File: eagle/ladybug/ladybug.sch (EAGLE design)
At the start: 4 parts

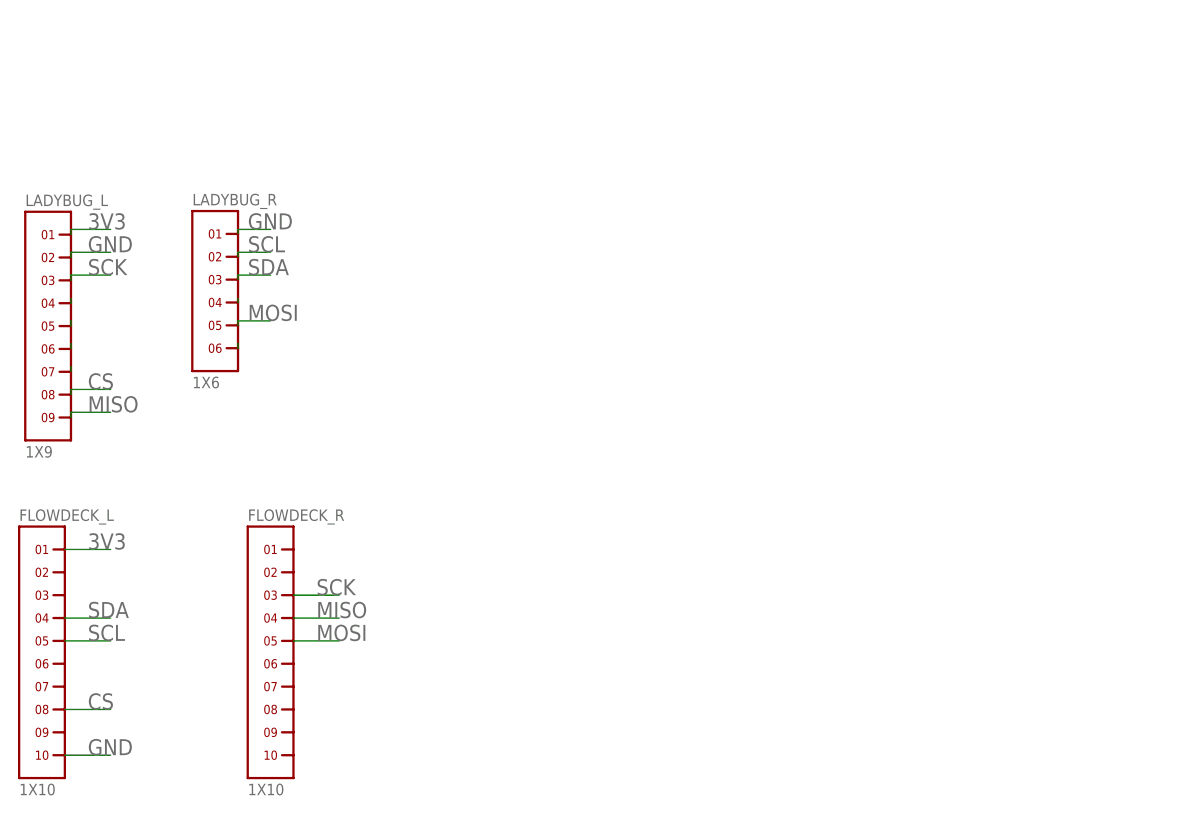
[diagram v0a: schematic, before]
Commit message: Added TinyPICO Nano to Ladybug board
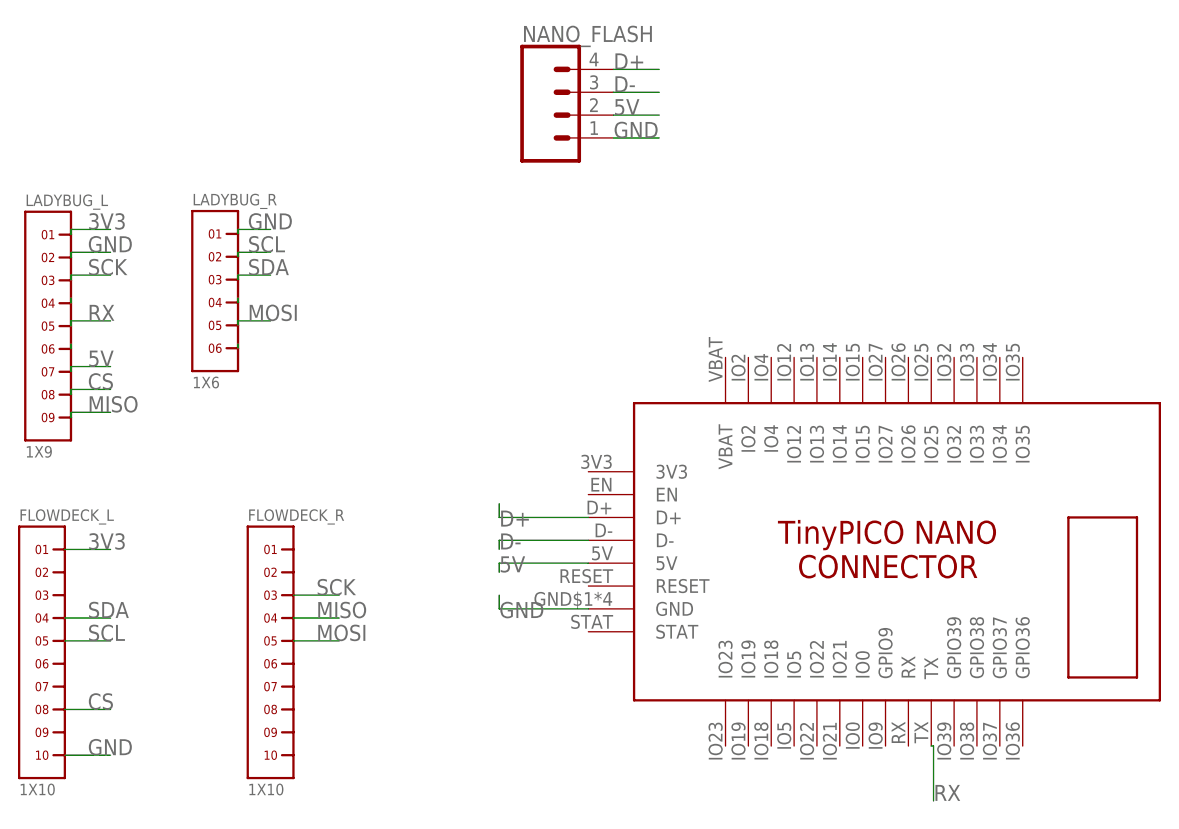
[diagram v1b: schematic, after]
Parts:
- added NANO_FLASH: (no value), SparkFun-Connectors:CONN_041X04_NO_SILK
- added U$1: TINYPICO-NANO-CONNECTOR, TinyPICO_NANO_Eagle:TINYPICO-NANO-CONNECTOR
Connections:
- removed net RX2: LADYBUG_L.5
- new net D+: NANO_FLASH.4, U$1.D+
- new net D-: NANO_FLASH.3, U$1.D-
- new net RX: LADYBUG_L.5, U$1.TX
- net 5V: now also NANO_FLASH.2, U$1.5V
- net GND: now also NANO_FLASH.1, U$1.GND
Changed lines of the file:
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@@
 <?xml version="1.0" encoding="utf-8"?>
 <!DOCTYPE eagle SYSTEM "eagle.dtd">
-<eagle version="9.1.1">
+<eagle version="9.6.2">
 <drawing>
 <settings>
@@
 <layer number="56" name="wert" color="7" fill="1" visible="no" active="no"/>
 <layer number="57" name="tCAD" color="7" fill="1" visible="no" active="no"/>
+<layer number="58" name="bCAD" color="7" fill="1" visible="no" active="no"/>
 <layer number="59" name="tCarbon" color="7" fill="1" visible="no" active="no"/>
 <layer number="60" name="bCarbon" color="7" fill="1" visible="no" active="no"/>
@@
 <layer number="115" name="ReferenceISLANDS" color="7" fill="1" visible="yes" active="yes"/>
 <layer number="116" name="Patch_BOT" color="9" fill="4" visible="yes" active="yes"/>
+<layer number="117" name="BACKMAAT1" color="7" fill="1" visible="no" active="no"/>
 <layer number="118" name="Rect_Pads" color="7" fill="1" visible="yes" active="yes"/>
+<layer number="119" name="KAP_TEKEN" color="7" fill="1" visible="no" active="no"/>
+<layer number="120" name="KAP_MAAT1" color="7" fill="1" visible="no" active="no"/>
 <layer number="121" name="_tsilk" color="7" fill="1" visible="yes" active="yes"/>
 <layer number="122" name="_bsilk" color="7" fill="1" visible="yes" active="yes"/>
@@
 <layer number="128" name="_bValues" color="7" fill="1" visible="yes" active="yes"/>
 <layer number="129" name="Mask" color="7" fill="1" visible="yes" active="yes"/>
+<layer number="130" name="SMDSTROOK" color="7" fill="1" visible="no" active="no"/>
 <layer number="131" name="tAdjust" color="7" fill="1" visible="yes" active="yes"/>
 <layer number="132" name="bAdjust" color="7" fill="1" visible="yes" active="yes"/>
+<layer number="133" name="bottom_silk" color="7" fill="1" visible="no" active="no"/>
+<layer number="134" name="silk_top" color="7" fill="1" visible="no" active="no"/>
+<layer number="135" name="silk_bottom" color="7" fill="1" visible="no" active="no"/>
+<layer number="136" name="silktop" color="7" fill="1" visible="yes" active="yes"/>
+<layer number="137" name="silkbottom" color="7" fill="1" visible="yes" active="yes"/>
+<layer number="138" name="mbTest" color="7" fill="1" visible="no" active="yes"/>
+<layer number="139" name="mtKeepout" color="7" fill="1" visible="no" active="yes"/>
+<layer number="140" name="mbKeepout" color="7" fill="1" visible="no" active="yes"/>
+<layer number="141" name="mtRestrict" color="7" fill="1" visible="no" active="yes"/>
+<layer number="142" name="mbRestrict" color="7" fill="1" visible="no" active="yes"/>
+<layer number="143" name="mvRestrict" color="7" fill="1" visible="no" active="yes"/>
 <layer number="144" name="Drill_legend" color="7" fill="1" visible="yes" active="yes"/>
+<layer number="145" name="DrillLegend_01-16" color="7" fill="1" visible="yes" active="yes"/>
+<layer number="146" name="DrillLegend_01-20" color="7" fill="1" visible="yes" active="yes"/>
+<layer number="147" name="mMeasures" color="7" fill="1" visible="no" active="yes"/>
+<layer number="148" name="mDocument" color="7" fill="1" visible="no" active="yes"/>
+<layer number="149" name="mReference" color="7" fill="1" visible="no" active="yes"/>
 <layer number="150" name="Notes" color="7" fill="1" visible="yes" active="yes"/>
 <layer number="151" name="HeatSink" color="7" fill="1" visible="yes" active="yes"/>
@@
 <layer number="154" name="FabDoc2" color="7" fill="1" visible="yes" active="yes"/>
 <layer number="155" name="FabDoc3" color="7" fill="1" visible="yes" active="yes"/>
+<layer number="156" name="gesam-Maß" color="7" fill="1" visible="no" active="no"/>
+<layer number="157" name="FaceMchng" color="7" fill="1" visible="no" active="no"/>
+<layer number="158" name="FaceMMeas" color="7" fill="1" visible="no" active="no"/>
+<layer number="159" name="Geh-Bear2" color="7" fill="1" visible="no" active="no"/>
+<layer number="160" name="Topologie" color="7" fill="1" visible="no" active="no"/>
+<layer number="161" name="tomplace2" color="7" fill="1" visible="no" active="no"/>
+<layer number="166" name="AntennaArea" color="7" fill="1" visible="yes" active="yes"/>
+<layer number="168" name="4mmHeightArea" color="7" fill="1" visible="yes" active="yes"/>
+<layer number="191" name="mNets" color="7" fill="1" visible="no" active="yes"/>
+<layer number="192" name="mBusses" color="7" fill="1" visible="no" active="yes"/>
+<layer number="193" name="mPins" color="7" fill="1" visible="no" active="yes"/>
+<layer number="194" name="mSymbols" color="7" fill="1" visible="no" active="yes"/>
+<layer number="195" name="mNames" color="7" fill="1" visible="no" active="yes"/>
+<layer number="196" name="mValues" color="7" fill="1" visible="no" active="yes"/>
 <layer number="199" name="Contour" color="7" fill="1" visible="yes" active="yes"/>
 <layer number="200" name="200bmp" color="1" fill="10" visible="yes" active="yes"/>
@@
 <layer number="250" name="Descript" color="3" fill="1" visible="no" active="no"/>
 <layer number="251" name="SMDround" color="12" fill="11" visible="no" active="no"/>
+<layer number="252" name="BR-BS" color="7" fill="1" visible="no" active="no"/>
+<layer number="253" name="Extra" color="7" fill="1" visible="no" active="no"/>
 <layer number="254" name="cooling" color="7" fill="1" visible="yes" active="yes"/>
 <layer number="255" name="routoute" color="7" fill="1" visible="yes" active="yes"/>
@@
 <part name="FLOWDECK_L" library="headers(2mm)" deviceset="1X10" device=""/>
 <part name="FLOWDECK_R" library="headers(2mm)" deviceset="1X10" device=""/>
+<part name="U$1" library="TinyPICO_NANO_Eagle" deviceset="TINYPICO-NANO-CONNECTOR" device=""/>
+<part name="NANO_FLASH" library="SparkFun-Connectors" deviceset="CONN_04" device="1X04_NO_SILK"/>
 </parts>
 <sheets>
@@
 <attribute name="VALUE" x="10.16" y="18.415" size="1.27" layer="96" font="vector"/>
 </instance>
+<instance part="U$1" gate="G$1" x="81.28" y="45.72" smashed="yes"/>
+<instance part="NANO_FLASH" gate="J1" x="45.72" y="93.98" smashed="yes">
+<attribute name="VALUE" x="40.64" y="86.614" size="1.778" layer="96" font="vector"/>
+<attribute name="NAME" x="40.64" y="102.108" size="1.778" layer="95" font="vector"/>
+</instance>
 </instances>
 <busses>
@@
 <pinref part="LADYBUG_L" gate="G$1" pin="7"/>
 <wire x1="-9.48" y1="65.46" x2="-9.48" y2="66.04" width="0.1524" layer="91"/>
-</segment>
-</net>
-<net name="RX2" class="0">
+<wire x1="-9.48" y1="66.04" x2="-5.08" y2="66.04" width="0.1524" layer="91"/>
+<label x="-7.62" y="66.04" size="1.778" layer="95"/>
+</segment>
+<segment>
+<pinref part="U$1" gate="G$1" pin="5V"/>
+<wire x1="48.006" y1="44.196" x2="38.1" y2="44.196" width="0.1524" layer="91"/>
+<wire x1="38.1" y1="44.196" x2="38.1" y2="43.18" width="0.1524" layer="91"/>
+<label x="38.1" y="43.18" size="1.778" layer="95"/>
+</segment>
+<segment>
+<pinref part="NANO_FLASH" gate="J1" pin="2"/>
+<wire x1="50.8" y1="93.98" x2="55.88" y2="93.98" width="0.1524" layer="91"/>
+<label x="50.8" y="93.98" size="1.778" layer="95"/>
+</segment>
+</net>
+<net name="RX" class="0">
 <segment>
 <pinref part="LADYBUG_L" gate="G$1" pin="5"/>
 <wire x1="-9.48" y1="70.54" x2="-9.48" y2="71.12" width="0.1524" layer="91"/>
+<wire x1="-9.48" y1="71.12" x2="-5.08" y2="71.12" width="0.1524" layer="91"/>
+<label x="-7.62" y="71.12" size="1.778" layer="95"/>
+</segment>
+<segment>
+<pinref part="U$1" gate="G$1" pin="TX"/>
+<wire x1="86.106" y1="23.876" x2="86.36" y2="23.876" width="0.1524" layer="91"/>
+<wire x1="86.36" y1="23.876" x2="86.36" y2="17.78" width="0.1524" layer="91"/>
+<label x="86.36" y="17.78" size="1.778" layer="95"/>
 </segment>
 </net>
@@
 <label x="-7.62" y="22.86" size="1.778" layer="95"/>
 </segment>
+<segment>
+<pinref part="U$1" gate="G$1" pin="GND"/>
+<wire x1="48.006" y1="39.116" x2="38.1" y2="39.116" width="0.1524" layer="91"/>
+<wire x1="38.1" y1="39.116" x2="38.1" y2="40.64" width="0.1524" layer="91"/>
+<label x="38.1" y="38.1" size="1.778" layer="95"/>
+</segment>
+<segment>
+<pinref part="NANO_FLASH" gate="J1" pin="1"/>
+<wire x1="50.8" y1="91.44" x2="55.88" y2="91.44" width="0.1524" layer="91"/>
+<label x="50.8" y="91.44" size="1.778" layer="95"/>
+</segment>
 </net>
 <net name="TX1" class="0">
@@
 <wire x1="9.08" y1="71.12" x2="12.7" y2="71.12" width="0.1524" layer="91"/>
 <label x="10.16" y="71.12" size="1.778" layer="95"/>
+</segment>
+</net>
+<net name="D-" class="0">
+<segment>
+<pinref part="U$1" gate="G$1" pin="D-"/>
+<wire x1="48.006" y1="46.736" x2="38.1" y2="46.736" width="0.1524" layer="91"/>
+<wire x1="38.1" y1="46.736" x2="38.1" y2="45.72" width="0.1524" layer="91"/>
+<label x="38.1" y="45.72" size="1.778" layer="95"/>
+</segment>
+<segment>
+<pinref part="NANO_FLASH" gate="J1" pin="3"/>
+<wire x1="50.8" y1="96.52" x2="55.88" y2="96.52" width="0.1524" layer="91"/>
+<label x="50.8" y="96.52" size="1.778" layer="95"/>
+</segment>
+</net>
+<net name="D+" class="0">
+<segment>
+<pinref part="U$1" gate="G$1" pin="D+"/>
+<wire x1="48.006" y1="49.276" x2="38.1" y2="49.276" width="0.1524" layer="91"/>
+<wire x1="38.1" y1="49.276" x2="38.1" y2="50.8" width="0.1524" layer="91"/>
+<label x="38.1" y="48.26" size="1.778" layer="95"/>
+</segment>
+<segment>
+<pinref part="NANO_FLASH" gate="J1" pin="4"/>
+<wire x1="50.8" y1="99.06" x2="55.88" y2="99.06" width="0.1524" layer="91"/>
+<label x="50.8" y="99.06" size="1.778" layer="95"/>
 </segment>
 </net>
@@
 </schematic>
 </drawing>
+<compatibility>
+<note version="6.3" minversion="6.2.2" severity="warning">
+Since Version 6.2.2 text objects can contain more than one line,
+which will not be processed correctly with this version.
+</note>
+</compatibility>
 </eagle>

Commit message: Ordered Ladybug Full Monte
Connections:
- new net RX2: LADYBUG_L.5, U$1.IO4
- net RX: no longer LADYBUG_L.5
- net TX2: now also U$1.IO2
